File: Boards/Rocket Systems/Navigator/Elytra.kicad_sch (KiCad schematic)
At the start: 23 parts, among them IC4 LMV321LILT, U10 NCR321UX, U11 NCR321UX, U9 NCR321UX

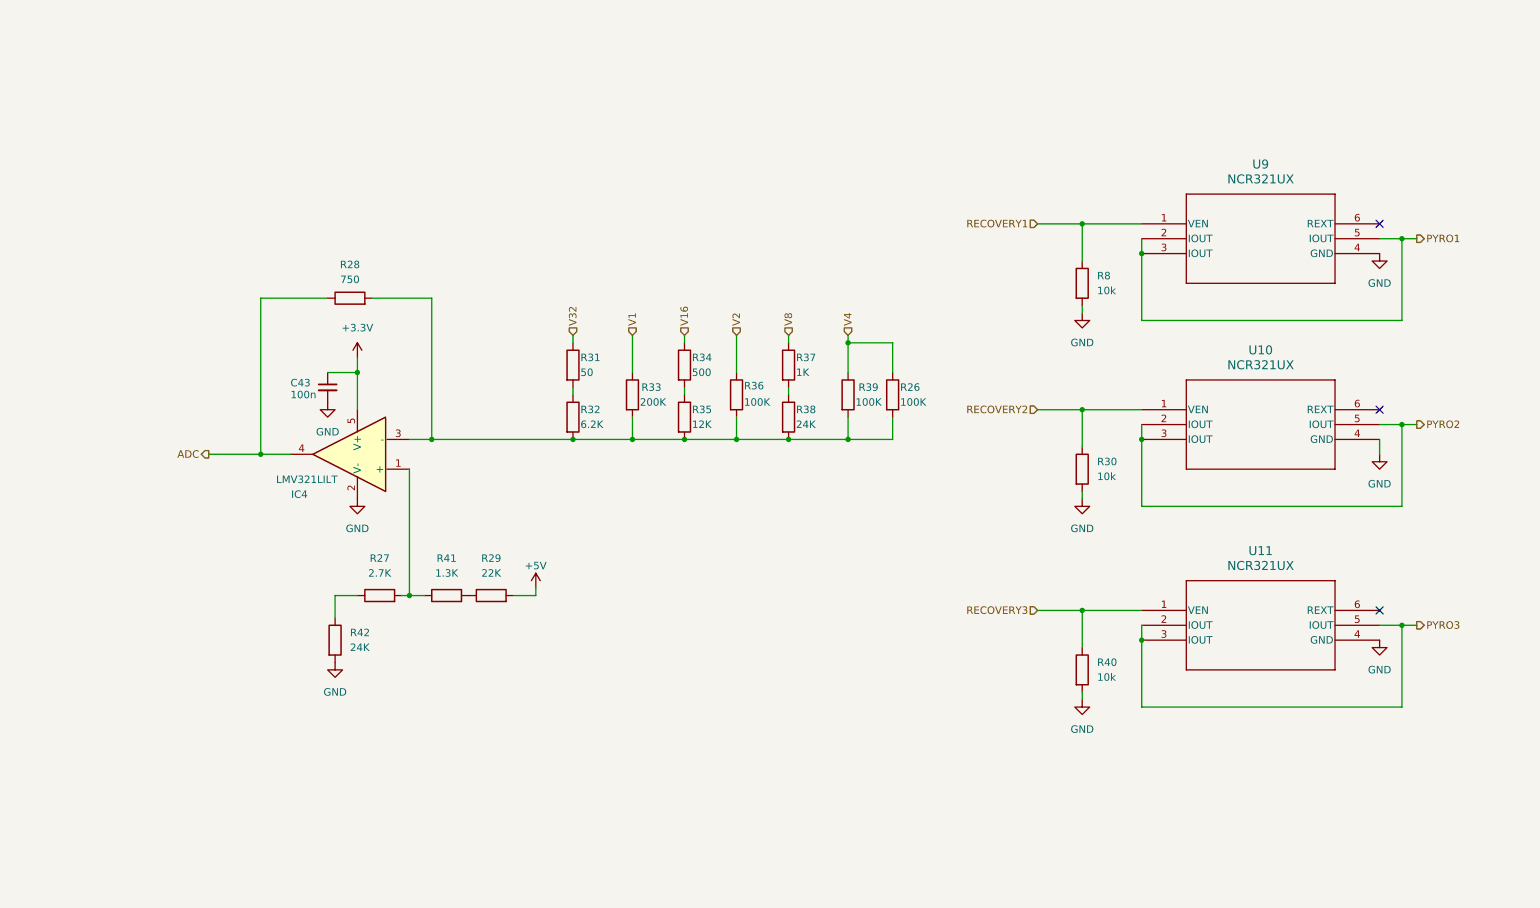
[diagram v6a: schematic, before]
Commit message: OBC, Nav, PocketSat review - SPI and I2C mistakes corrected
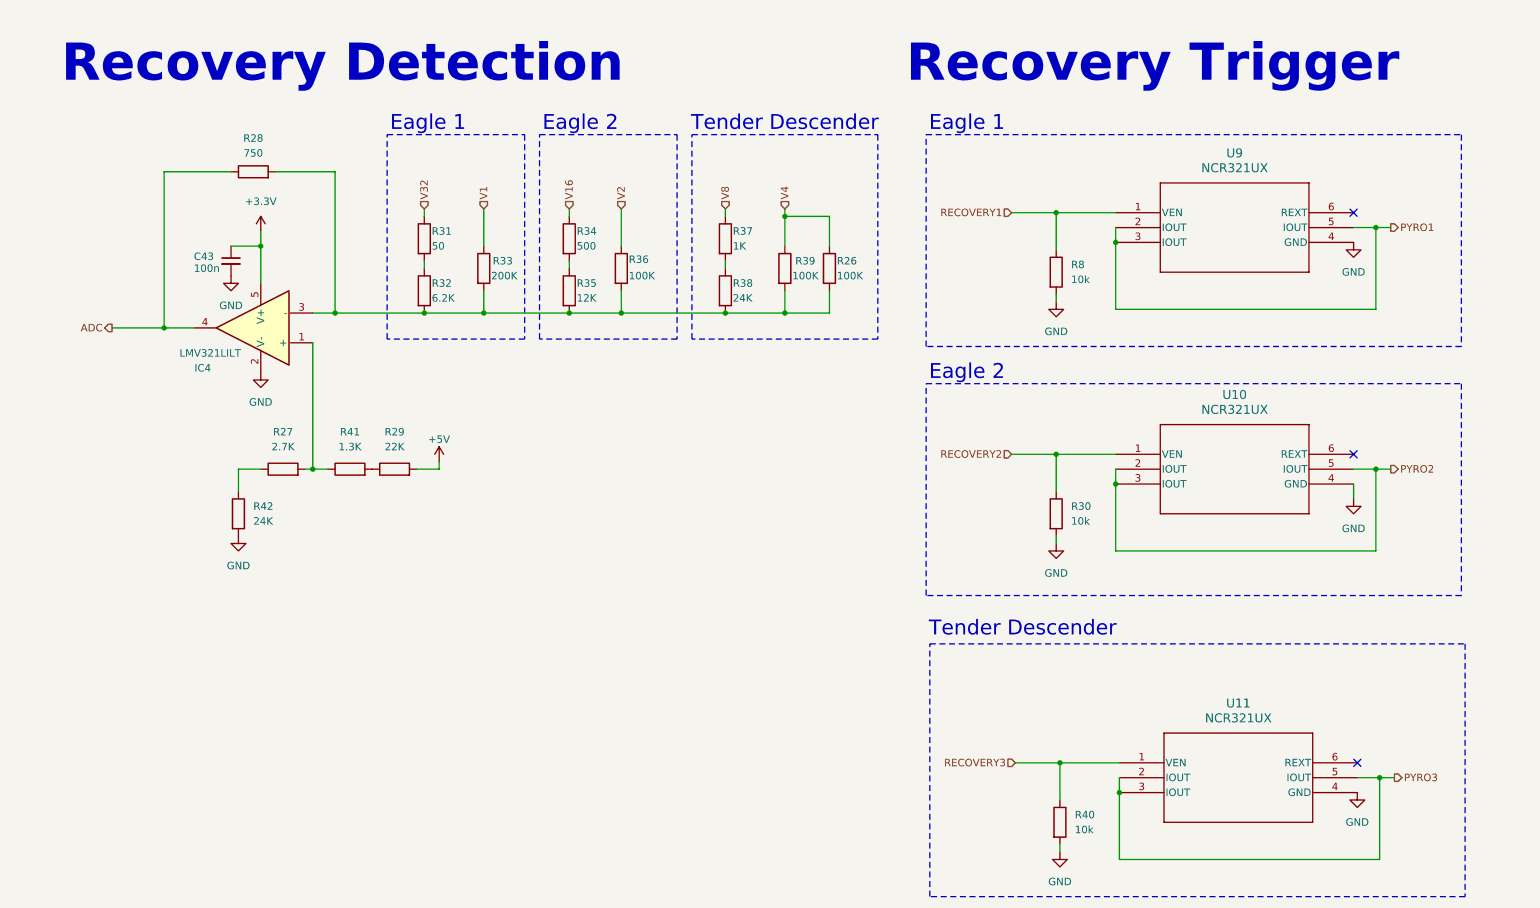
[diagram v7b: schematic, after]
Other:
- note added: "Eagle 1"
- note added: "Eagle 2"
- note added: "Recovery Detection"
- note added: "Recovery Trigger"
- note added: "Tender Descender"
- moved on the sheet: C43, IC4, R26, R27, R28, R29, R30, R31, R32, R33, R34, R35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

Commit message: HYDRA Schematic Update Final Touches
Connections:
- net V16 is gone; now on net V4: R34.1
- net V1: now also R36.1; no longer R33.1
- net V2: now also R26.1, R39.1; no longer R36.1
- net V4: no longer R26.1, R39.1
- net V32 renamed V5
- net V8 renamed V3
- new net V0: R33.1
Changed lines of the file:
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@@
 	(rectangle
 		(start 120.015 31.75)
-		(end 151.765 66.675)
+		(end 152.4 66.675)
 		(stroke
 			(width 0)
@@
 		)
 	)
-	(hierarchical_label "V2"
+	(hierarchical_label "V1"
 		(shape input)
 		(at 107.95 44.45 90)
@@
 		)
 	)
-	(hierarchical_label "V8"
+	(hierarchical_label "V3"
 		(shape input)
 		(at 125.73 44.45 90)
@@
 		)
 	)
-	(hierarchical_label "V4"
+	(hierarchical_label "V2"
 		(shape input)
 		(at 135.89 44.45 90)
@@
 		)
 	)
-	(hierarchical_label "V32"
+	(hierarchical_label "V5"
 		(shape input)
 		(at 74.295 44.45 90)
@@
 		)
 	)
-	(hierarchical_label "V1"
+	(hierarchical_label "V0"
 		(shape input)
 		(at 84.455 44.45 90)
@@
 		)
 	)
-	(hierarchical_label "V16"
+	(hierarchical_label "V4"
 		(shape input)
 		(at 99.06 44.45 90)
